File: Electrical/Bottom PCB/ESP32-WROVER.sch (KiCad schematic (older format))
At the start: 13 parts, among them J201 PROGRAMMING, J202 MainIO, Q201 BC847, Q202 BC847, U201 ESP32-WROVER

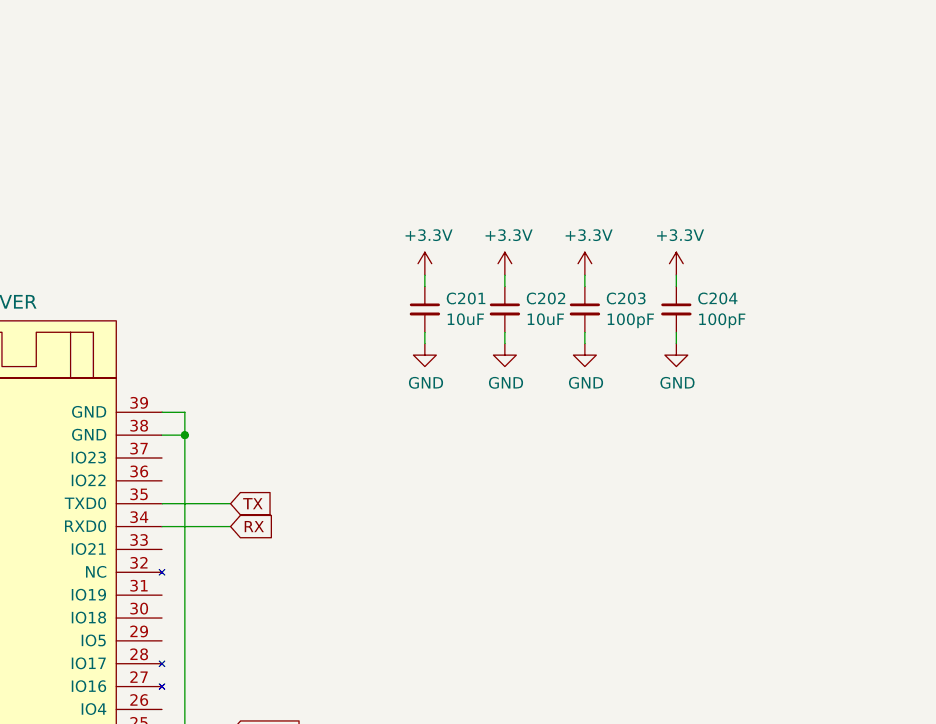
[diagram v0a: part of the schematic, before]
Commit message: Set up MCP23017
Added the main parts of an MCP23017
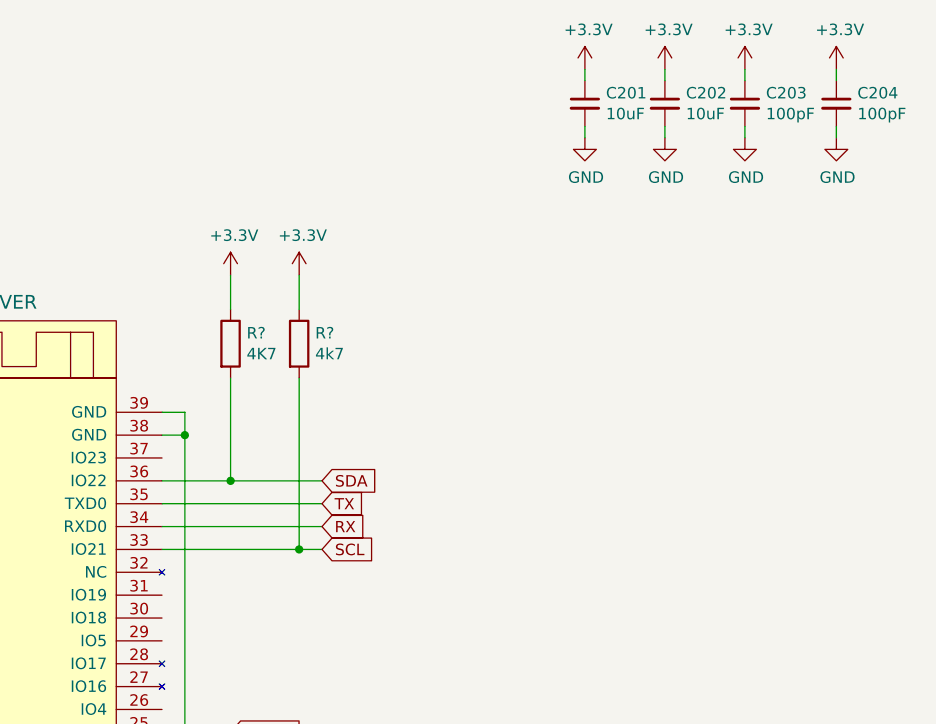
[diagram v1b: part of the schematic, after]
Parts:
- added R?: 4K7, Resistor_SMD:R_1206_3216Metric_Pad1.42x1.75mm_HandSolder, symbol Device:R
- added R?: 4k7, Resistor_SMD:R_1206_3216Metric_Pad1.42x1.75mm_HandSolder, symbol Device:R
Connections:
- net labels added: SCL, SDA
- wire segments 70 -> 78
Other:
- moved on the sheet: C201, C202, C203, C204

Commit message: simplified the pcb,
Removed the shift registers and moved functionality onto the 16 way IO expander, also removed the H-Bridge, may re-add a I2C duel h-bridge at a later date.

Thinking about best way to drive the four servo headers, may use I2C controller for them as well, as then the timing maths is removed from the main micro
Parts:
- gave numbers to parts that had none: 2
- renumbered R201 to R203, R202 to R204
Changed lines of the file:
@@
 P 8200 4350
 AR Path="/5EBD2BE0" Ref="#PWR?"  Part="1"
-AR Path="/5EBB31C5/5EBD2BE0" Ref="#PWR0216"  Part="1"
-F 0 "#PWR0216" H 8200 4100 50  0001 C CNN
+AR Path="/5EBB31C5/5EBD2BE0" Ref="#PWR0218"  Part="1"
+F 0 "#PWR0218" H 8200 4100 50  0001 C CNN
 F 1 "GND" H 8205 4177 50  0000 C CNN
 F 2 "" H 8200 4350 50  0001 C CNN
@@
 P 6250 4350
 AR Path="/5EBD2BE6" Ref="#PWR?"  Part="1"
-AR Path="/5EBB31C5/5EBD2BE6" Ref="#PWR0215"  Part="1"
-F 0 "#PWR0215" H 6250 4100 50  0001 C CNN
+AR Path="/5EBB31C5/5EBD2BE6" Ref="#PWR0217"  Part="1"
+F 0 "#PWR0217" H 6250 4100 50  0001 C CNN
 F 1 "GND" H 6255 4177 50  0000 C CNN
 F 2 "" H 6250 4350 50  0001 C CNN
@@
 P 6200 1500
 AR Path="/5EBD2BEC" Ref="#PWR?"  Part="1"
-AR Path="/5EBB31C5/5EBD2BEC" Ref="#PWR0202"  Part="1"
-F 0 "#PWR0202" H 6200 1350 50  0001 C CNN
+AR Path="/5EBB31C5/5EBD2BEC" Ref="#PWR0210"  Part="1"
+F 0 "#PWR0210" H 6200 1350 50  0001 C CNN
 F 1 "+3.3V" H 6215 1673 50  0000 C CNN
 F 2 "" H 6200 1500 50  0001 C CNN
@@
 P 1600 2700
 AR Path="/5EBF7F71" Ref="#PWR?"  Part="1"
-AR Path="/5EBB31C5/5EBF7F71" Ref="#PWR0211"  Part="1"
-F 0 "#PWR0211" H 1600 2450 50  0001 C CNN
+AR Path="/5EBB31C5/5EBF7F71" Ref="#PWR0213"  Part="1"
+F 0 "#PWR0213" H 1600 2450 50  0001 C CNN
 F 1 "GND" H 1605 2527 50  0000 C CNN
 F 2 "" H 1600 2700 50  0001 C CNN
@@
 P 1500 1500
 AR Path="/5EBF7F79" Ref="#PWR?"  Part="1"
-AR Path="/5EBB31C5/5EBF7F79" Ref="#PWR0201"  Part="1"
-F 0 "#PWR0201" H 1500 1350 50  0001 C CNN
+AR Path="/5EBB31C5/5EBF7F79" Ref="#PWR0209"  Part="1"
+F 0 "#PWR0209" H 1500 1350 50  0001 C CNN
 F 1 "+3.3V" H 1515 1673 50  0000 C CNN
 F 2 "" H 1500 1500 50  0001 C CNN
@@
 P 2200 2250
 AR Path="/5EBF7F98" Ref="R?"  Part="1"
-AR Path="/5EBB31C5/5EBF7F98" Ref="R201"  Part="1"
-F 0 "R201" H 2270 2296 50  0000 L CNN
+AR Path="/5EBB31C5/5EBF7F98" Ref="R203"  Part="1"
+F 0 "R203" H 2270 2296 50  0000 L CNN
 F 1 "10K" H 2270 2205 50  0000 L CNN
 F 2 "Resistor_SMD:R_1206_3216Metric_Pad1.42x1.75mm_HandSolder" V 2130 2250 50  0001 C CNN
@@
 P 2950 2250
 AR Path="/5EBF7F9E" Ref="R?"  Part="1"
-AR Path="/5EBB31C5/5EBF7F9E" Ref="R202"  Part="1"
-F 0 "R202" H 3020 2296 50  0000 L CNN
+AR Path="/5EBB31C5/5EBF7F9E" Ref="R204"  Part="1"
+F 0 "R204" H 3020 2296 50  0000 L CNN
 F 1 "10K" H 3020 2205 50  0000 L CNN
 F 2 "Resistor_SMD:R_1206_3216Metric_Pad1.42x1.75mm_HandSolder" V 2880 2250 50  0001 C CNN
@@
 P 1950 3750
 AR Path="/5EC352F2" Ref="#PWR?"  Part="1"
-AR Path="/5EBB31C5/5EC352F2" Ref="#PWR0214"  Part="1"
-F 0 "#PWR0214" H 1950 3600 50  0001 C CNN
+AR Path="/5EBB31C5/5EC352F2" Ref="#PWR0216"  Part="1"
+F 0 "#PWR0216" H 1950 3600 50  0001 C CNN
 F 1 "+5V" H 1965 3923 50  0000 C CNN
 F 2 "" H 1950 3750 50  0001 C CNN
@@
 P 1600 4900
 AR Path="/5EC35302" Ref="#PWR?"  Part="1"
-AR Path="/5EBB31C5/5EC35302" Ref="#PWR0217"  Part="1"
-F 0 "#PWR0217" H 1600 4650 50  0001 C CNN
+AR Path="/5EBB31C5/5EC35302" Ref="#PWR0219"  Part="1"
+F 0 "#PWR0219" H 1600 4650 50  0001 C CNN
 F 1 "GND" H 1605 4727 50  0000 C CNN
 F 2 "" H 1600 4900 50  0001 C CNN
@@
 P 1700 3750
 AR Path="/5EC35309" Ref="#PWR?"  Part="1"
-AR Path="/5EBB31C5/5EC35309" Ref="#PWR0213"  Part="1"
-F 0 "#PWR0213" H 1700 3600 50  0001 C CNN
+AR Path="/5EBB31C5/5EC35309" Ref="#PWR0215"  Part="1"
+F 0 "#PWR0215" H 1700 3600 50  0001 C CNN
 F 1 "+BATT" H 1715 3923 50  0000 C CNN
 F 2 "" H 1700 3750 50  0001 C CNN
@@
 P 11050 900
 AR Path="/5ECDAD45" Ref="#PWR?"  Part="1"
-AR Path="/5EBB31C5/5ECDAD45" Ref="#PWR0210"  Part="1"
-F 0 "#PWR0210" H 11050 650 50  0001 C CNN
+AR Path="/5EBB31C5/5ECDAD45" Ref="#PWR0208"  Part="1"
+F 0 "#PWR0208" H 11050 650 50  0001 C CNN
 F 1 "GND" H 11055 727 50  0000 C CNN
 F 2 "" H 11050 900 50  0001 C CNN
@@
 P 9950 900
 AR Path="/5ECDAD53" Ref="#PWR?"  Part="1"
-AR Path="/5EBB31C5/5ECDAD53" Ref="#PWR0207"  Part="1"
-F 0 "#PWR0207" H 9950 650 50  0001 C CNN
+AR Path="/5EBB31C5/5ECDAD53" Ref="#PWR0205"  Part="1"
+F 0 "#PWR0205" H 9950 650 50  0001 C CNN
 F 1 "GND" H 9955 727 50  0000 C CNN
 F 2 "" H 9950 900 50  0001 C CNN
@@
 P 10300 600
 AR Path="/5ECDAD5B" Ref="#PWR?"  Part="1"
-AR Path="/5EBB31C5/5ECDAD5B" Ref="#PWR0204"  Part="1"
-F 0 "#PWR0204" H 10300 450 50  0001 C CNN
+AR Path="/5EBB31C5/5ECDAD5B" Ref="#PWR0202"  Part="1"
+F 0 "#PWR0202" H 10300 450 50  0001 C CNN
 F 1 "+3.3V" H 10315 773 50  0000 C CNN
 F 2 "" H 10300 600 50  0001 C CNN
@@
 P 10650 600
 AR Path="/5ECDAD6D" Ref="#PWR?"  Part="1"
-AR Path="/5EBB31C5/5ECDAD6D" Ref="#PWR0205"  Part="1"
-F 0 "#PWR0205" H 10650 450 50  0001 C CNN
+AR Path="/5EBB31C5/5ECDAD6D" Ref="#PWR0203"  Part="1"
+F 0 "#PWR0203" H 10650 450 50  0001 C CNN
 F 1 "+3.3V" H 10665 773 50  0000 C CNN
 F 2 "" H 10650 600 50  0001 C CNN
@@
 P 10300 900
 AR Path="/5ECDAD73" Ref="#PWR?"  Part="1"
-AR Path="/5EBB31C5/5ECDAD73" Ref="#PWR0208"  Part="1"
-F 0 "#PWR0208" H 10300 650 50  0001 C CNN
+AR Path="/5EBB31C5/5ECDAD73" Ref="#PWR0206"  Part="1"
+F 0 "#PWR0206" H 10300 650 50  0001 C CNN
 F 1 "GND" H 10305 727 50  0000 C CNN
 F 2 "" H 10300 900 50  0001 C CNN
@@
 P 10650 900
 AR Path="/5ECDAD79" Ref="#PWR?"  Part="1"
-AR Path="/5EBB31C5/5ECDAD79" Ref="#PWR0209"  Part="1"
-F 0 "#PWR0209" H 10650 650 50  0001 C CNN
+AR Path="/5EBB31C5/5ECDAD79" Ref="#PWR0207"  Part="1"
+F 0 "#PWR0207" H 10650 650 50  0001 C CNN
 F 1 "GND" H 10655 727 50  0000 C CNN
 F 2 "" H 10650 900 50  0001 C CNN
@@
 P 11050 600
 AR Path="/5ECDAD7F" Ref="#PWR?"  Part="1"
-AR Path="/5EBB31C5/5ECDAD7F" Ref="#PWR0206"  Part="1"
-F 0 "#PWR0206" H 11050 450 50  0001 C CNN
+AR Path="/5EBB31C5/5ECDAD7F" Ref="#PWR0204"  Part="1"
+F 0 "#PWR0204" H 11050 450 50  0001 C CNN
 F 1 "+3.3V" H 11065 773 50  0000 C CNN
 F 2 "" H 11050 600 50  0001 C CNN
@@
 P 9950 600
 AR Path="/5ECDAD85" Ref="#PWR?"  Part="1"
-AR Path="/5EBB31C5/5ECDAD85" Ref="#PWR0203"  Part="1"
-F 0 "#PWR0203" H 9950 450 50  0001 C CNN
+AR Path="/5EBB31C5/5ECDAD85" Ref="#PWR0201"  Part="1"
+F 0 "#PWR0201" H 9950 450 50  0001 C CNN
 F 1 "+3.3V" H 9965 773 50  0000 C CNN
 F 2 "" H 9950 600 50  0001 C CNN
@@
 TX_sw
 $Comp
-L power:+3V8 #PWR0212
+L power:+3V8 #PWR0214
 U 1 1 5ED4BDA3
 P 1450 3750
-F 0 "#PWR0212" H 1450 3600 50  0001 C CNN
+F 0 "#PWR0214" H 1450 3600 50  0001 C CNN
 F 1 "+3V8" H 1465 3923 50  0000 C CNN
 F 2 "" H 1450 3750 50  0001 C CNN
@@
 P 8400 1800
 AR Path="/5EBEB5DB" Ref="R?"  Part="1"
-AR Path="/5EBB31C5/5EBEB5DB" Ref="R?"  Part="1"
-F 0 "R?" H 8470 1846 50  0000 L CNN
+AR Path="/5EBB31C5/5EBEB5DB" Ref="R201"  Part="1"
+F 0 "R201" H 8470 1846 50  0000 L CNN
 F 1 "4K7" H 8470 1755 50  0000 L CNN
 F 2 "Resistor_SMD:R_1206_3216Metric_Pad1.42x1.75mm_HandSolder" V 8330 1800 50  0001 C CNN
@@
 P 8700 1800
 AR Path="/5EBFDF19" Ref="R?"  Part="1"
-AR Path="/5EBB31C5/5EBFDF19" Ref="R?"  Part="1"
-F 0 "R?" H 8770 1846 50  0000 L CNN
+AR Path="/5EBB31C5/5EBFDF19" Ref="R202"  Part="1"
+F 0 "R202" H 8770 1846 50  0000 L CNN
 F 1 "4k7" H 8770 1755 50  0000 L CNN
 F 2 "Resistor_SMD:R_1206_3216Metric_Pad1.42x1.75mm_HandSolder" V 8630 1800 50  0001 C CNN
@@
 P 8400 1500
 AR Path="/5EBFE3A2" Ref="#PWR?"  Part="1"
-AR Path="/5EBB31C5/5EBFE3A2" Ref="#PWR?"  Part="1"
-F 0 "#PWR?" H 8400 1350 50  0001 C CNN
+AR Path="/5EBB31C5/5EBFE3A2" Ref="#PWR0211"  Part="1"
+F 0 "#PWR0211" H 8400 1350 50  0001 C CNN
 F 1 "+3.3V" H 8415 1673 50  0000 C CNN
 F 2 "" H 8400 1500 50  0001 C CNN
@@
 P 8700 1500
 AR Path="/5EBFEB1D" Ref="#PWR?"  Part="1"
-AR Path="/5EBB31C5/5EBFEB1D" Ref="#PWR?"  Part="1"
-F 0 "#PWR?" H 8700 1350 50  0001 C CNN
+AR Path="/5EBB31C5/5EBFEB1D" Ref="#PWR0212"  Part="1"
+F 0 "#PWR0212" H 8700 1350 50  0001 C CNN
 F 1 "+3.3V" H 8715 1673 50  0000 C CNN
 F 2 "" H 8700 1500 50  0001 C CNN

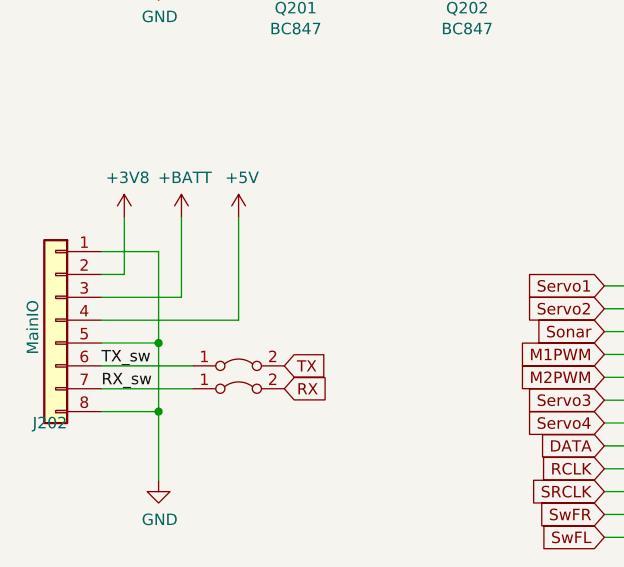
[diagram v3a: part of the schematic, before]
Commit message: Added power switch
Some more modifications
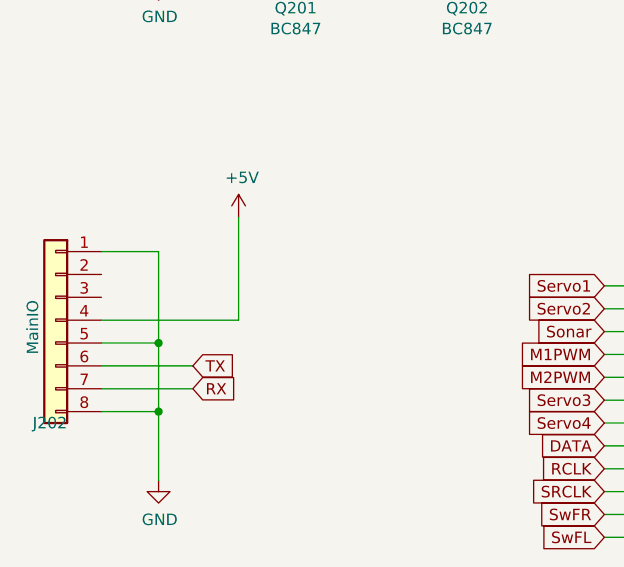
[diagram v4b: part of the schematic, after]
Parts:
- removed JP201, JP202: Jumper_2_Bridged, Jumper:SolderJumper-2_P1.3mm_Bridged2Bar_Pad1.0x1.5mm, symbol Jumper:Jumper_2_Bridged
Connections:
- net labels removed: +3V8, +BATT, RX_sw, TX_sw
- wire segments 78 -> 74
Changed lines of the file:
@@
 $Descr A4 11693 8268
 encoding utf-8
-Sheet 2 4
+Sheet 2 3
 Title ""
 Date ""
@@
 Wire Wire Line
 	1350 4400 1750 4400
-Text GLabel 2150 4500 2    49   Input ~ 0
+Text GLabel 1750 4500 2    49   Input ~ 0
 RX
-Text GLabel 2150 4400 2    49   Input ~ 0
+Text GLabel 1750 4400 2    49   Input ~ 0
 TX
 $Comp
@@
 Wire Wire Line
 	1350 4200 1950 4200
-$Comp
-L power:+BATT #PWR?
-U 1 1 5EC35309
-P 1700 3750
-AR Path="/5EC35309" Ref="#PWR?"  Part="1"
-AR Path="/5EBB31C5/5EC35309" Ref="#PWR0215"  Part="1"
-F 0 "#PWR0215" H 1700 3600 50  0001 C CNN
-F 1 "+BATT" H 1715 3923 50  0000 C CNN
-F 2 "" H 1700 3750 50  0001 C CNN
-F 3 "" H 1700 3750 50  0001 C CNN
-	1    1700 3750
-	1    0    0    -1
-$EndComp
 Wire Wire Line
 	1600 4300 1600 4600
-Wire Wire Line
-	1350 4100 1700 4100
 Wire Wire Line
 	1950 4200 1950 3750
@@
 Wire Wire Line
 	1350 4500 1750 4500
-Wire Wire Line
-	1700 3750 1700 4100
 $Comp
 L Connector_Generic:Conn_01x06 J?
@@
 $EndComp
 $Comp
-L Jumper:Jumper_2_Bridged JP201
-U 1 1 5EC5A549
-P 1950 4400
-F 0 "JP201" H 1950 4595 50  0001 C CNN
-F 1 "Jumper_2_Bridged" H 1950 4504 50  0001 C CNN
-F 2 "Jumper:SolderJumper-2_P1.3mm_Bridged2Bar_Pad1.0x1.5mm" H 1950 4400 50  0001 C CNN
-F 3 "~" H 1950 4400 50  0001 C CNN
-	1    1950 4400
-	1    0    0    -1
-$EndComp
-$Comp
-L Jumper:Jumper_2_Bridged JP202
-U 1 1 5EC5AE21
-P 1950 4500
-F 0 "JP202" H 1950 4695 50  0001 C CNN
-F 1 "Jumper_2_Bridged" H 1950 4604 50  0001 C CNN
-F 2 "Jumper:SolderJumper-2_P1.3mm_Bridged2Bar_Pad1.0x1.5mm" H 1950 4500 50  0001 C CNN
-F 3 "~" H 1950 4500 50  0001 C CNN
-	1    1950 4500
-	1    0    0    -1
-$EndComp
-$Comp
 L Device:C_Small C?
 U 1 1 5ECDAD3F
@@
 Wire Wire Line
 	10300 850  10300 900
-Text Label 1350 4500 0    50   ~ 0
-RX_sw
-Text Label 1350 4400 0    50   ~ 0
-TX_sw
-$Comp
-L power:+3V8 #PWR0214
-U 1 1 5ED4BDA3
-P 1450 3750
-F 0 "#PWR0214" H 1450 3600 50  0001 C CNN
-F 1 "+3V8" H 1465 3923 50  0000 C CNN
-F 2 "" H 1450 3750 50  0001 C CNN
-F 3 "" H 1450 3750 50  0001 C CNN
-	1    1450 3750
-	1    0    0    -1
-$EndComp
-Wire Wire Line
-	1450 3750 1450 4000
-Wire Wire Line
-	1450 4000 1350 4000
 Wire Wire Line
 	1600 4300 1600 3900

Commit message: changed from 1206 to 0805
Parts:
- C201, C202, C203, C204: footprint Capacitor_SMD:C_1206_3216Metric_Pad1.42x1.75mm_HandSolder -> Capacitor_SMD:C_0805_2012Metric_Pad1.15x1.40mm_HandSolder
- J202: footprint Connector_PinHeader_2.54mm:PinHeader_1x08_P2.54mm_Vertical -> Connector_PinHeader_2.54mm:PinHeader_1x06_P2.54mm_Vertical; symbol Connector_Generic:Conn_01x08 -> Connector_Generic:Conn_01x06
- R201, R202, R203, R204: footprint Resistor_SMD:R_1206_3216Metric_Pad1.42x1.75mm_HandSolder -> Resistor_SMD:R_0805_2012Metric_Pad1.15x1.40mm_HandSolder
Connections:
- net labels added: 5V_Switched, Sonar_Echo, Sonar_Trig
- net labels removed: Sonar
- wire segments 74 -> 75
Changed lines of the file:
@@
 F 0 "R203" H 2270 2296 50  0000 L CNN
 F 1 "10K" H 2270 2205 50  0000 L CNN
-F 2 "Resistor_SMD:R_1206_3216Metric_Pad1.42x1.75mm_HandSolder" V 2130 2250 50  0001 C CNN
+F 2 "Resistor_SMD:R_0805_2012Metric_Pad1.15x1.40mm_HandSolder" V 2130 2250 50  0001 C CNN
 F 3 "~" H 2200 2250 50  0001 C CNN
 	1    2200 2250
@@
 F 0 "R204" H 3020 2296 50  0000 L CNN
 F 1 "10K" H 3020 2205 50  0000 L CNN
-F 2 "Resistor_SMD:R_1206_3216Metric_Pad1.42x1.75mm_HandSolder" V 2880 2250 50  0001 C CNN
+F 2 "Resistor_SMD:R_0805_2012Metric_Pad1.15x1.40mm_HandSolder" V 2880 2250 50  0001 C CNN
 F 3 "~" H 2950 2250 50  0001 C CNN
 	1    2950 2250
@@
 Wire Wire Line
 	3700 4050 3550 4050
-Text GLabel 6000 2400 0    50   Input ~ 0
+Text GLabel 6000 2500 0    50   Input ~ 0
 BatV
 Wire Wire Line
 	4500 4900 4350 4900
-Text GLabel 3550 4250 0    50   Input ~ 0
-Sonar
 Wire Wire Line
 	4500 4500 4350 4500
@@
 Wire Wire Line
 	1600 1600 1600 2700
-$Comp
-L power:+5V #PWR?
-U 1 1 5EC352F2
-P 1950 3750
-AR Path="/5EC352F2" Ref="#PWR?"  Part="1"
-AR Path="/5EBB31C5/5EC352F2" Ref="#PWR0214"  Part="1"
-F 0 "#PWR0214" H 1950 3600 50  0001 C CNN
-F 1 "+5V" H 1965 3923 50  0000 C CNN
-F 2 "" H 1950 3750 50  0001 C CNN
-F 3 "" H 1950 3750 50  0001 C CNN
-	1    1950 3750
-	1    0    0    -1
-$EndComp
-Wire Wire Line
-	1350 4300 1600 4300
-Wire Wire Line
-	1350 4400 1750 4400
-Text GLabel 1750 4500 2    49   Input ~ 0
+Wire Wire Line
+	1350 4300 1400 4300
+Wire Wire Line
+	1350 4400 1550 4400
+Text GLabel 1550 4500 2    49   Input ~ 0
 RX
-Text GLabel 1750 4400 2    49   Input ~ 0
+Text GLabel 1550 4400 2    49   Input ~ 0
 TX
 $Comp
 L power:GND #PWR?
 U 1 1 5EC35302
-P 1600 4900
+P 1400 4700
 AR Path="/5EC35302" Ref="#PWR?"  Part="1"
 AR Path="/5EBB31C5/5EC35302" Ref="#PWR0217"  Part="1"
-F 0 "#PWR0217" H 1600 4650 50  0001 C CNN
-F 1 "GND" H 1605 4727 50  0000 C CNN
-F 2 "" H 1600 4900 50  0001 C CNN
-F 3 "" H 1600 4900 50  0001 C CNN
-	1    1600 4900
-	1    0    0    -1
-$EndComp
-Wire Wire Line
-	1350 4200 1950 4200
-Wire Wire Line
-	1600 4300 1600 4600
-Wire Wire Line
-	1950 4200 1950 3750
-Wire Wire Line
-	1350 4600 1600 4600
-Connection ~ 1600 4600
-Wire Wire Line
-	1600 4600 1600 4900
-Wire Wire Line
-	1350 4500 1750 4500
+F 0 "#PWR0217" H 1400 4450 50  0001 C CNN
+F 1 "GND" H 1405 4527 50  0000 C CNN
+F 2 "" H 1400 4700 50  0001 C CNN
+F 3 "" H 1400 4700 50  0001 C CNN
+	1    1400 4700
+	1    0    0    -1
+$EndComp
+Wire Wire Line
+	1400 4300 1400 4600
+Wire Wire Line
+	1350 4600 1400 4600
+Connection ~ 1400 4600
+Wire Wire Line
+	1400 4600 1400 4700
+Wire Wire Line
+	1350 4500 1550 4500
 $Comp
 L Connector_Generic:Conn_01x06 J?
@@
 $EndComp
 $Comp
-L Connector_Generic:Conn_01x08 J?
-U 1 1 5EC352F8
-P 1150 4200
-AR Path="/5EC352F8" Ref="J?"  Part="1"
-AR Path="/5EBB31C5/5EC352F8" Ref="J202"  Part="1"
-F 0 "J202" H 1100 3750 50  0000 L CNN
-F 1 "MainIO" V 1250 4050 50  0000 L CNN
-F 2 "Connector_PinHeader_2.54mm:PinHeader_1x08_P2.54mm_Vertical" H 1150 4200 50  0001 C CNN
-F 3 "~" H 1150 4200 50  0001 C CNN
-	1    1150 4200
-	-1   0    0    -1
-$EndComp
-$Comp
 L Device:C_Small C?
 U 1 1 5ECDAD3F
@@
 F 0 "C204" H 11142 796 50  0000 L CNN
 F 1 "100pF" H 11142 705 50  0000 L CNN
-F 2 "Capacitor_SMD:C_1206_3216Metric_Pad1.42x1.75mm_HandSolder" H 11050 750 50  0001 C CNN
+F 2 "Capacitor_SMD:C_0805_2012Metric_Pad1.15x1.40mm_HandSolder" H 11050 750 50  0001 C CNN
 F 3 "~" H 11050 750 50  0001 C CNN
 	1    11050 750
@@
 F 0 "C201" H 10042 796 50  0000 L CNN
 F 1 "10uF" H 10042 705 50  0000 L CNN
-F 2 "Capacitor_SMD:C_1206_3216Metric_Pad1.42x1.75mm_HandSolder" H 9950 750 50  0001 C CNN
+F 2 "Capacitor_SMD:C_0805_2012Metric_Pad1.15x1.40mm_HandSolder" H 9950 750 50  0001 C CNN
 F 3 "~" H 9950 750 50  0001 C CNN
 	1    9950 750
@@
 F 0 "C202" H 10392 796 50  0000 L CNN
 F 1 "10uF" H 10392 705 50  0000 L CNN
-F 2 "Capacitor_SMD:C_1206_3216Metric_Pad1.42x1.75mm_HandSolder" H 10300 750 50  0001 C CNN
+F 2 "Capacitor_SMD:C_0805_2012Metric_Pad1.15x1.40mm_HandSolder" H 10300 750 50  0001 C CNN
 F 3 "~" H 10300 750 50  0001 C CNN
 	1    10300 750
@@
 F 0 "C203" H 10742 796 50  0000 L CNN
 F 1 "100pF" H 10742 705 50  0000 L CNN
-F 2 "Capacitor_SMD:C_1206_3216Metric_Pad1.42x1.75mm_HandSolder" H 10650 750 50  0001 C CNN
+F 2 "Capacitor_SMD:C_0805_2012Metric_Pad1.15x1.40mm_HandSolder" H 10650 750 50  0001 C CNN
 F 3 "~" H 10650 750 50  0001 C CNN
 	1    10650 750
@@
 Wire Wire Line
 	10300 850  10300 900
-Wire Wire Line
-	1600 4300 1600 3900
-Wire Wire Line
-	1600 3900 1350 3900
-Connection ~ 1600 4300
-Text GLabel 6000 2500 0    50   Input ~ 0
+Text GLabel 6000 2400 0    50   Input ~ 0
 half_BatV
 Wire Wire Line
@@
 F 0 "R201" H 8470 1846 50  0000 L CNN
 F 1 "4K7" H 8470 1755 50  0000 L CNN
-F 2 "Resistor_SMD:R_1206_3216Metric_Pad1.42x1.75mm_HandSolder" V 8330 1800 50  0001 C CNN
+F 2 "Resistor_SMD:R_0805_2012Metric_Pad1.15x1.40mm_HandSolder" V 8330 1800 50  0001 C CNN
 F 3 "~" H 8400 1800 50  0001 C CNN
 	1    8400 1800
@@
 F 0 "R202" H 8770 1846 50  0000 L CNN
 F 1 "4k7" H 8770 1755 50  0000 L CNN
-F 2 "Resistor_SMD:R_1206_3216Metric_Pad1.42x1.75mm_HandSolder" V 8630 1800 50  0001 C CNN
+F 2 "Resistor_SMD:R_0805_2012Metric_Pad1.15x1.40mm_HandSolder" V 8630 1800 50  0001 C CNN
 F 3 "~" H 8700 1800 50  0001 C CNN
 	1    8700 1800
@@
 Wire Wire Line
 	8400 2400 8800 2400
+Text GLabel 6000 2700 0    50   Input ~ 0
+Sonar_Trig
+Text GLabel 6000 2600 0    50   Input ~ 0
+Sonar_Echo
+Wire Wire Line
+	6000 2600 6350 2600
+Wire Wire Line
+	6350 2700 6000 2700
+Wire Wire Line
+	1350 4200 1450 4200
+Wire Wire Line
+	1450 4200 1450 4050
+$Comp
+L power:+5V #PWR?
+U 1 1 5EC352F2
+P 1450 4050
+AR Path="/5EC352F2" Ref="#PWR?"  Part="1"
+AR Path="/5EBB31C5/5EC352F2" Ref="#PWR0214"  Part="1"
+F 0 "#PWR0214" H 1450 3900 50  0001 C CNN
+F 1 "+5V" H 1465 4223 50  0000 C CNN
+F 2 "" H 1450 4050 50  0001 C CNN
+F 3 "" H 1450 4050 50  0001 C CNN
+	1    1450 4050
+	1    0    0    -1
+$EndComp
+$Comp
+L Connector_Generic:Conn_01x06 J?
+U 1 1 5EC352F8
+P 1150 4300
+AR Path="/5EC352F8" Ref="J?"  Part="1"
+AR Path="/5EBB31C5/5EC352F8" Ref="J202"  Part="1"
+F 0 "J202" H 1100 3850 50  0000 L CNN
+F 1 "MainIO" V 1250 4150 50  0000 L CNN
+F 2 "Connector_PinHeader_2.54mm:PinHeader_1x06_P2.54mm_Vertical" H 1150 4300 50  0001 C CNN
+F 3 "~" H 1150 4300 50  0001 C CNN
+	1    1150 4300
+	-1   0    0    -1
+$EndComp
+Text GLabel 1550 4100 2    50   Input ~ 0
+5V_Switched
+Wire Wire Line
+	1350 4100 1550 4100
 $EndSCHEMATC
